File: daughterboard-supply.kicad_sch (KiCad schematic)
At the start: 18 parts, among them J9 39281103, U15 AP62301WU-7, U4 AP62301WU-7

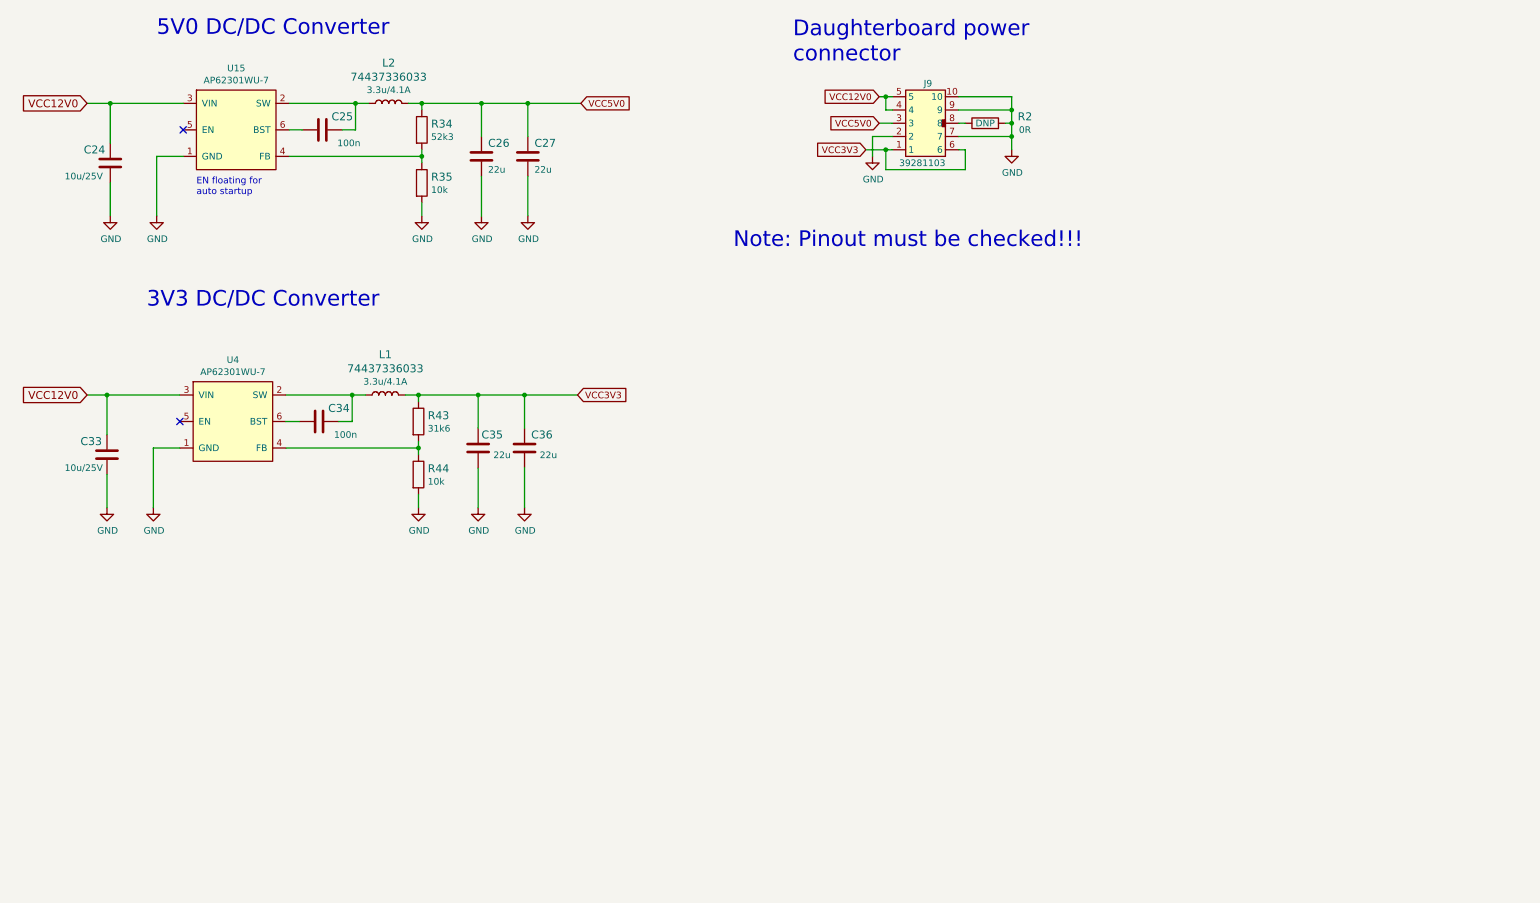
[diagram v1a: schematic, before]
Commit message: Add photo, unify the size of schematic sheets
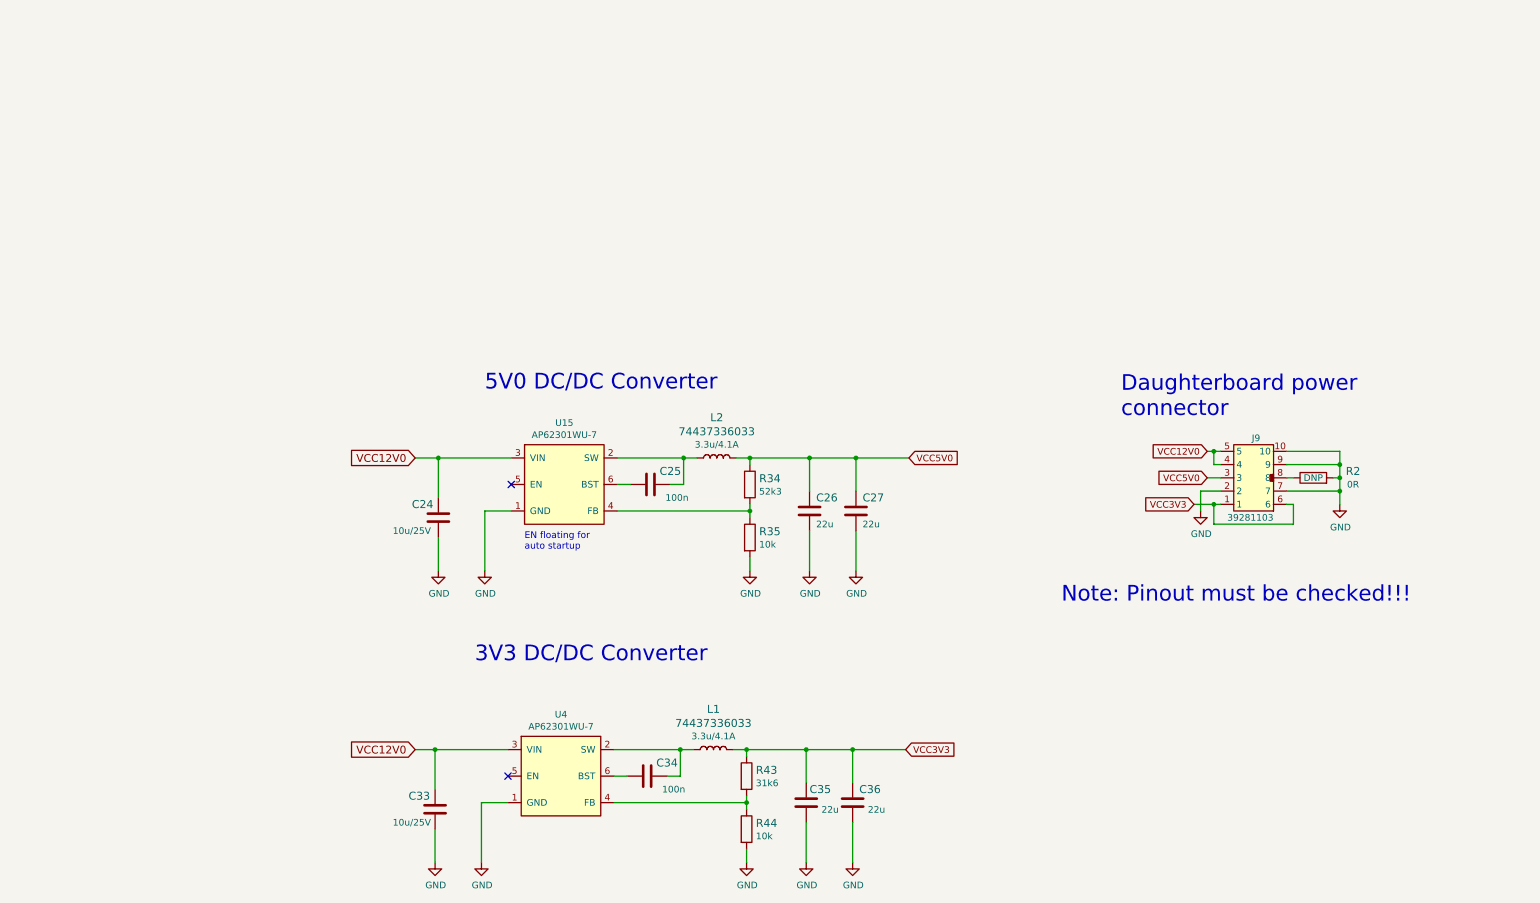
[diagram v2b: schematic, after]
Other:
- moved on the sheet: C24, C25, C26, C27, C33, C34, C35, C36, J9, L1, L2, R2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

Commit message: Update README
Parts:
- C24, C33: footprint nuc-compute-cluster-power-breakout-footprints:0603-cap -> d1600e-psu-breakout-board-footprints:0603-cap; symbol nuc-compute-cluster-power-breakout:C_10u_25V_0603 -> d1600e-psu-breakout-board:C_10u_25V_0603
- C25, C34: footprint nuc-compute-cluster-power-breakout-footprints:0402-cap -> d1600e-psu-breakout-board-footprints:0402-cap; symbol nuc-compute-cluster-power-breakout:C_100n_0402 -> d1600e-psu-breakout-board:C_100n_0402
- C26, C27, C35, C36: footprint nuc-compute-cluster-power-breakout-footprints:0603-cap -> d1600e-psu-breakout-board-footprints:0603-cap; symbol nuc-compute-cluster-power-breakout:C_22u_0603 -> d1600e-psu-breakout-board:C_22u_0603
- J9: footprint nuc-compute-cluster-power-breakout-footprints:MOLEX_39281103 -> d1600e-psu-breakout-board-footprints:MOLEX_39281103; symbol nuc-compute-cluster-power-breakout:39281103 -> d1600e-psu-breakout-board:39281103
- L1, L2: footprint nuc-compute-cluster-power-breakout-footprints:WE_74437336033 -> d1600e-psu-breakout-board-footprints:WE_74437336033; symbol nuc-compute-cluster-power-breakout:74437336033 -> d1600e-psu-breakout-board:74437336033
- R2: footprint nuc-compute-cluster-power-breakout-footprints:0402-res -> d1600e-psu-breakout-board-footprints:0402-res; symbol nuc-compute-cluster-power-breakout:R_0R_0402 -> d1600e-psu-breakout-board:R_0R_0402
- R34: footprint nuc-compute-cluster-power-breakout-footprints:0402-res -> d1600e-psu-breakout-board-footprints:0402-res; symbol nuc-compute-cluster-power-breakout:R_52k3_0402 -> d1600e-psu-breakout-board:R_52k3_0402
- R35, R44: footprint nuc-compute-cluster-power-breakout-footprints:0402-res -> d1600e-psu-breakout-board-footprints:0402-res; symbol nuc-compute-cluster-power-breakout:R_10k_0402 -> d1600e-psu-breakout-board:R_10k_0402
- R43: footprint nuc-compute-cluster-power-breakout-footprints:0402-res -> d1600e-psu-breakout-board-footprints:0402-res; symbol nuc-compute-cluster-power-breakout:R_31k6_0402 -> d1600e-psu-breakout-board:R_31k6_0402
- U15, U4: footprint nuc-compute-cluster-power-breakout-footprints:TSOT23-6 -> d1600e-psu-breakout-board-footprints:TSOT23-6; symbol nuc-compute-cluster-power-breakout:AP62301WU-7 -> d1600e-psu-breakout-board:AP62301WU-7
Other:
- title: NUC Computer Cluster Power Breakout HW -> D1600E PSU Breakout Board

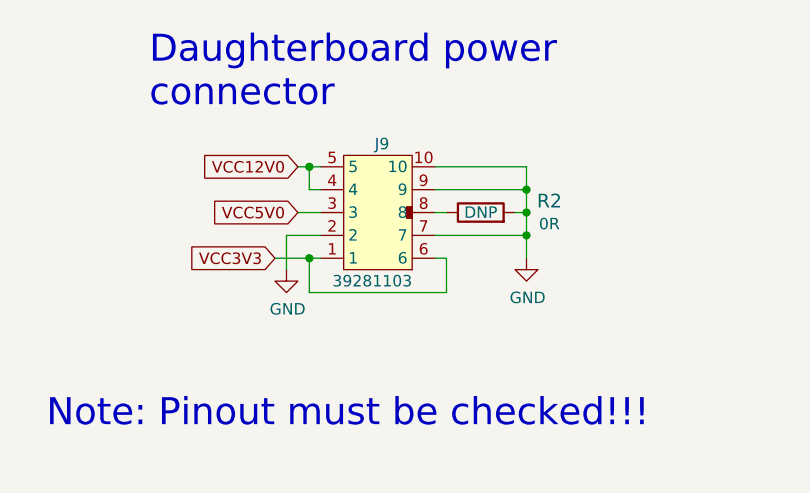
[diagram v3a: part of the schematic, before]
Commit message: Added protection for I2C, fix resistor value for USB C, Fixed J9 reversed polarity, minor width fix to 3v3 line
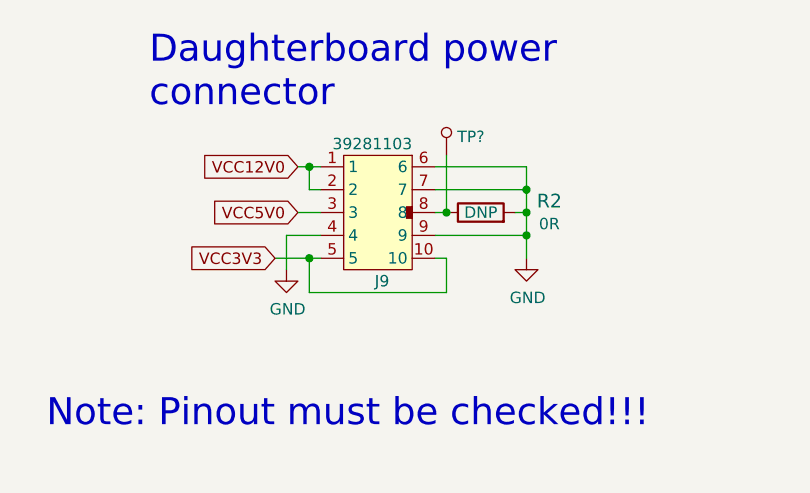
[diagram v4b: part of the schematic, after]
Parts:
- added TP?: TP_SMD1MM, antmicro-footprints:Testpoint_smd_1mm, symbol antmicroTestPoints:TP_SMD1MM
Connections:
- net GND: now also J9.4, J9.6; no longer J9.10, J9.2
- net VCC12V0: now also J9.1, J9.2; no longer J9.4, J9.5
- net VCC3V3: now also J9.10, J9.5; no longer J9.1, J9.6
- net at J9.8, R2.1: now also TP?.1
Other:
- moved on the sheet: J9
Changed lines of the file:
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@@
   (junction (at 295.275 114.935) (diameter 0) (color 0 0 0 0)
   )
+  (junction (at 286.385 117.475) (diameter 0) (color 0 0 0 0)
+  )
   (junction (at 168.91 169.545) (diameter 0) (color 0 0 0 0)
   )
@@
     (stroke (width 0) (type default) (color 0 0 0 0))
   )
+  (wire (pts (xy 286.385 111.125) (xy 286.385 117.475))
+    (stroke (width 0) (type default) (color 0 0 0 0))
+  )
   (wire (pts (xy 168.91 169.545) (xy 171.45 169.545))
     (stroke (width 0) (type default) (color 0 0 0 0))
@@
     (pin "1")
   )
-  (symbol (lib_id "d1600e-psu-breakout-board:39281103") (at 278.765 118.745 180) (unit 1)
+  (symbol (lib_id "antmicroTestPoints:TP_SMD1MM") (at 286.385 108.585 180) (unit 1)
+    (in_bom yes) (on_board yes) (fields_autoplaced)
+    (property "Reference" "TP?" (id 0) (at 287.5788 109.0569 0)
+      (effects (font (size 1.27 1.27)) (justify right))
+    )
+    (property "Value" "TP_SMD1MM" (id 1) (at 286.385 106.045 0)
+      (effects (font (size 1.27 1.27)) hide)
+    )
+    (property "Footprint" "antmicro-footprints:Testpoint_smd_1mm" (id 2) (at 281.305 113.665 0)
+      (effects (font (size 1.524 1.524)) (justify left) hide)
+    )
+    (property "Datasheet" "" (id 3) (at 281.305 116.205 0)
+      (effects (font (size 1.524 1.524)) (justify left) hide)
+    )
+    (pin "1")
+  )
+  (symbol (lib_id "d1600e-psu-breakout-board:39281103") (at 278.765 116.205 0) (mirror y) (unit 1)
     (in_bom yes) (on_board yes)
-    (property "Reference" "J9" (id 0) (at 280.035 109.855 0)
+    (property "Reference" "J9" (id 0) (at 280.035 125.095 0)
       (effects (font (size 1.27 1.27)) (justify left))
     )
-    (property "Value" "39281103" (id 1) (at 282.575 125.095 0)
+    (property "Value" "39281103" (id 1) (at 282.575 109.855 0)
       (effects (font (size 1.27 1.27)) (justify left))
     )
-    (property "Footprint" "d1600e-psu-breakout-board-footprints:MOLEX_39281103" (id 2) (at 278.765 95.885 0)
+    (property "Footprint" "d1600e-psu-breakout-board-footprints:MOLEX_39281103" (id 2) (at 278.765 139.065 0)
       (effects (font (size 1.27 1.27)) hide)
     )
-    (property "Datasheet" "https://www.molex.com/pdm_docs/sd/039281103_sd.pdf" (id 3) (at 277.495 98.425 0)
+    (property "Datasheet" "https://www.molex.com/pdm_docs/sd/039281103_sd.pdf" (id 3) (at 277.495 136.525 0)
       (effects (font (size 1.27 1.27)) hide)
     )
-    (property "MPN" "39281103" (id 4) (at 278.765 100.965 0)
+    (property "MPN" "39281103" (id 4) (at 278.765 133.985 0)
       (effects (font (size 1.27 1.27)) hide)
     )
-    (property "Manufacturer" "Molex" (id 5) (at 278.765 103.505 0)
+    (property "Manufacturer" "Molex" (id 5) (at 278.765 131.445 0)
       (effects (font (size 1.27 1.27)) hide)
     )

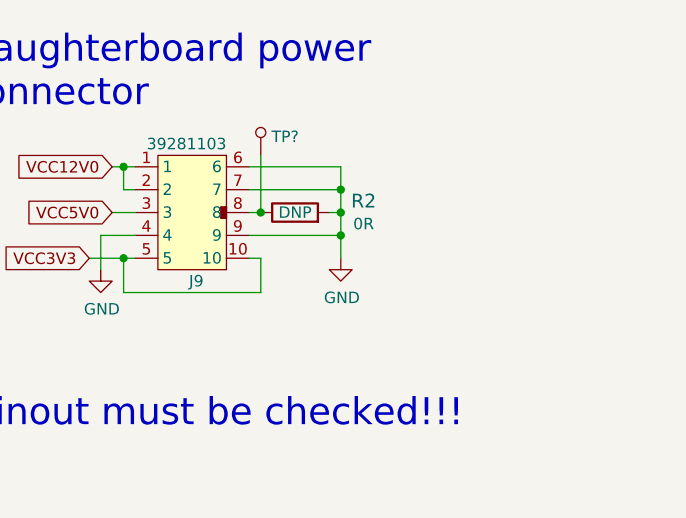
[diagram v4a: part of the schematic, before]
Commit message: Aded molex connectors for PCI-e risers and pul up down option for 5V info rail from coordinator
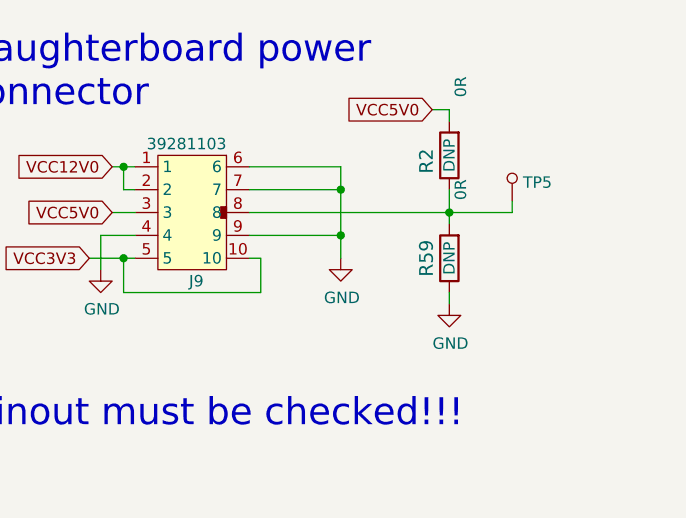
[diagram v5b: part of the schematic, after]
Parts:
- added R59: R_0R_0402, d1600e-psu-breakout-board-footprints:0402-res, symbol d1600e-psu-breakout-board:R_0R_0402
- gave numbers to parts that had none: 1
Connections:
- net GND: now also R59.1; no longer R2.2
- net VCC5V0: now also R2.2
- net at J9.8, R2.1, TP5.1: now also R59.2
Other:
- moved on the sheet: R2, TP5
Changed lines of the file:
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@@
     (comment 2 "Antmicro Ltd.")
   )
-  (junction (at 295.275 117.475) (diameter 0) (color 0 0 0 0)
-  )
   (junction (at 193.675 113.665) (diameter 0) (color 0 0 0 0)
   )
@@
   (junction (at 295.275 114.935) (diameter 0) (color 0 0 0 0)
   )
-  (junction (at 286.385 117.475) (diameter 0) (color 0 0 0 0)
-  )
   (junction (at 168.91 169.545) (diameter 0) (color 0 0 0 0)
   )
@@
   (junction (at 121.92 169.545) (diameter 0) (color 0 0 0 0)
   )
+  (junction (at 307.34 117.475) (diameter 0) (color 0 0 0 0)
+  )
   (junction (at 193.04 169.545) (diameter 0) (color 0 0 0 0)
   )
@@
     (stroke (width 0) (type default) (color 0 0 0 0))
   )
+  (wire (pts (xy 307.34 107.315) (xy 307.34 106.045))
+    (stroke (width 0) (type default) (color 0 0 0 0))
+  )
   (wire (pts (xy 122.555 113.665) (xy 136.525 113.665))
     (stroke (width 0) (type default) (color 0 0 0 0))
@@
     (stroke (width 0) (type default) (color 0 0 0 0))
   )
-  (wire (pts (xy 294.005 117.475) (xy 295.275 117.475))
-    (stroke (width 0) (type default) (color 0 0 0 0))
-  )
   (wire (pts (xy 159.385 118.745) (xy 156.845 118.745))
     (stroke (width 0) (type default) (color 0 0 0 0))
@@
     (stroke (width 0) (type default) (color 0 0 0 0))
   )
-  (wire (pts (xy 295.275 114.935) (xy 295.275 117.475))
+  (wire (pts (xy 295.275 114.935) (xy 295.275 120.015))
     (stroke (width 0) (type default) (color 0 0 0 0))
   )
@@
     (stroke (width 0) (type default) (color 0 0 0 0))
   )
-  (wire (pts (xy 295.275 117.475) (xy 295.275 120.015))
-    (stroke (width 0) (type default) (color 0 0 0 0))
-  )
   (wire (pts (xy 122.555 135.255) (xy 122.555 128.905))
     (stroke (width 0) (type default) (color 0 0 0 0))
@@
     (stroke (width 0) (type default) (color 0 0 0 0))
   )
+  (wire (pts (xy 307.34 114.935) (xy 307.34 117.475))
+    (stroke (width 0) (type default) (color 0 0 0 0))
+  )
+  (wire (pts (xy 314.325 117.475) (xy 307.34 117.475))
+    (stroke (width 0) (type default) (color 0 0 0 0))
+  )
+  (wire (pts (xy 307.34 126.365) (xy 307.34 127.635))
+    (stroke (width 0) (type default) (color 0 0 0 0))
+  )
+  (wire (pts (xy 307.34 117.475) (xy 307.34 118.745))
+    (stroke (width 0) (type default) (color 0 0 0 0))
+  )
   (wire (pts (xy 122.555 121.285) (xy 122.555 113.665))
     (stroke (width 0) (type default) (color 0 0 0 0))
@@
     (stroke (width 0) (type default) (color 0 0 0 0))
   )
-  (wire (pts (xy 286.385 111.125) (xy 286.385 117.475))
+  (wire (pts (xy 314.325 116.205) (xy 314.325 117.475))
     (stroke (width 0) (type default) (color 0 0 0 0))
   )
@@
     (stroke (width 0) (type default) (color 0 0 0 0))
   )
+  (wire (pts (xy 307.34 106.045) (xy 305.435 106.045))
+    (stroke (width 0) (type default) (color 0 0 0 0))
+  )
   (wire (pts (xy 169.545 118.745) (xy 169.545 113.665))
     (stroke (width 0) (type default) (color 0 0 0 0))
@@
     (stroke (width 0) (type default) (color 0 0 0 0))
   )
-  (wire (pts (xy 285.115 117.475) (xy 286.385 117.475))
+  (wire (pts (xy 285.115 117.475) (xy 307.34 117.475))
     (stroke (width 0) (type default) (color 0 0 0 0))
   )
@@
     )
   )
+  (global_label "VCC5V0" (shape input) (at 305.435 106.045 180) (fields_autoplaced)
+    (effects (font (size 1.27 1.27)) (justify right))
+    (property "Intersheet References" "${INTERSHEET_REFS}" (id 0) (at 71.755 48.895 0)
+      (effects (font (size 1.27 1.27)) hide)
+    )
+  )
   (symbol (lib_id "d1600e-psu-breakout-board:AP62301WU-7") (at 146.685 118.745 0) (unit 1)
     (in_bom yes) (on_board yes)
@@
     (pin "2")
   )
-  (symbol (lib_id "d1600e-psu-breakout-board:R_0R_0402") (at 290.195 117.475 0) (unit 1)
+  (symbol (lib_id "d1600e-psu-breakout-board:R_0R_0402") (at 307.34 111.125 90) (unit 1)
+    (in_bom yes) (on_board yes)
+    (property "Reference" "R2" (id 0) (at 304.8 111.76 0)
+      (effects (font (size 1.524 1.524)))
+    )
+    (property "Value" "R_0R_0402" (id 1) (at 311.15 111.125 0)
+      (effects (font (size 1.524 1.524)) hide)
+    )
+    (property "Footprint" "d1600e-psu-breakout-board-footprints:0402-res" (id 2) (at 302.26 106.045 0)
+      (effects (font (size 1.524 1.524)) (justify left) hide)
+    )
+    (property "Datasheet" "" (id 3) (at 307.34 111.125 0)
+      (effects (font (size 1.27 1.27)) hide)
+    )
+    (property "Manufacturer" "PANASONIC" (id 4) (at 297.18 106.045 0)
+      (effects (font (size 1.524 1.524)) (justify left) hide)
+    )
+    (property "MPN" "ERJ2GE0R00X" (id 5) (at 299.72 106.045 0)
+      (effects (font (size 1.524 1.524)) (justify left) hide)
+    )
+    (property "Val" "0R" (id 6) (at 308.61 103.505 0))
+    (property "DNP" "DNP" (id 7) (at 307.34 111.125 0))
+    (pin "1")
+    (pin "2")
+  )
+  (symbol (lib_id "d1600e-psu-breakout-board:GND") (at 307.34 127.635 0) (unit 1)
+    (in_bom yes) (on_board yes)
+    (property "Reference" "#PWR0135" (id 0) (at 307.34 133.985 0)
+      (effects (font (size 1.27 1.27)) hide)
+    )
+    (property "Value" "GND" (id 1) (at 307.467 132.0292 0))
+    (property "Footprint" "d1600e-psu-breakout-board-footprints:" (id 2) (at 307.34 127.635 0)
+      (effects (font (size 1.27 1.27)) hide)
+    )
+    (property "Datasheet" "" (id 3) (at 307.34 127.635 0)
+      (effects (font (size 1.27 1.27)) hide)
+    )
+    (pin "1")
+  )
+  (symbol (lib_id "d1600e-psu-breakout-board:R_0R_0402") (at 307.34 122.555 90) (unit 1)
     (in_bom yes) (on_board yes)
-    (property "Reference" "R2" (id 0) (at 297.815 116.205 0)
+    (property "Reference" "R59" (id 0) (at 304.8 122.555 0)
       (effects (font (size 1.524 1.524)))
     )
-    (property "Value" "R_0R_0402" (id 1) (at 290.195 121.285 0)
+    (property "Value" "R_0R_0402" (id 1) (at 311.15 122.555 0)
       (effects (font (size 1.524 1.524)) hide)
     )
-    (property "Footprint" "d1600e-psu-breakout-board-footprints:0402-res" (id 2) (at 295.275 112.395 0)
+    (property "Footprint" "d1600e-psu-breakout-board-footprints:0402-res" (id 2) (at 302.26 117.475 0)
       (effects (font (size 1.524 1.524)) (justify left) hide)
     )
-    (property "Datasheet" "" (id 3) (at 290.195 117.475 0)
+    (property "Datasheet" "" (id 3) (at 307.34 122.555 0)
       (effects (font (size 1.27 1.27)) hide)
     )
-    (property "Manufacturer" "PANASONIC" (id 4) (at 295.275 107.315 0)
+    (property "Manufacturer" "PANASONIC" (id 4) (at 297.18 117.475 0)
       (effects (font (size 1.524 1.524)) (justify left) hide)
     )
-    (property "MPN" "ERJ2GE0R00X" (id 5) (at 295.275 109.855 0)
+    (property "MPN" "ERJ2GE0R00X" (id 5) (at 299.72 117.475 0)
       (effects (font (size 1.524 1.524)) (justify left) hide)
     )
-    (property "Val" "0R" (id 6) (at 297.815 118.745 0))
-    (property "DNP" "DNP" (id 7) (at 290.195 117.475 0))
+    (property "Val" "0R" (id 6) (at 308.61 114.935 0))
+    (property "DNP" "DNP" (id 7) (at 307.34 122.555 0))
     (pin "1")
     (pin "2")
@@
     (pin "1")
   )
-  (symbol (lib_id "antmicroTestPoints:TP_SMD1MM") (at 286.385 108.585 180) (unit 1)
+  (symbol (lib_id "antmicroTestPoints:TP_SMD1MM") (at 314.325 113.665 180) (unit 1)
     (in_bom yes) (on_board yes) (fields_autoplaced)
-    (property "Reference" "TP?" (id 0) (at 287.5788 109.0569 0)
+    (property "Reference" "TP5" (id 0) (at 315.5188 114.1369 0)
       (effects (font (size 1.27 1.27)) (justify right))
     )
-    (property "Value" "TP_SMD1MM" (id 1) (at 286.385 106.045 0)
+    (property "Value" "TP_SMD1MM" (id 1) (at 314.325 111.125 0)
       (effects (font (size 1.27 1.27)) hide)
     )
-    (property "Footprint" "antmicro-footprints:Testpoint_smd_1mm" (id 2) (at 281.305 113.665 0)
+    (property "Footprint" "antmicro-footprints:Testpoint_smd_1mm" (id 2) (at 309.245 118.745 0)
       (effects (font (size 1.524 1.524)) (justify left) hide)
     )
-    (property "Datasheet" "" (id 3) (at 281.305 116.205 0)
+    (property "Datasheet" "" (id 3) (at 309.245 121.285 0)
       (effects (font (size 1.524 1.524)) (justify left) hide)
     )
